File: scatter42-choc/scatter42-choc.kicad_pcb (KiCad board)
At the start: 2 copper layers, 260.1 x 107.6 mm, 112 parts, among them J0 MJ-4PP-9, J1 MJ-4PP-9, SW0 SW_PUSH, SW1 SW_PUSH, SW10 SW_PUSH, SW11 SW_PUSH, SW12 SW_PUSH, SW13 SW_PUSH, SW14 SW_PUSH, SW15 SW_PUSH, SW16 SW_PUSH, SW17 SW_PUSH, SW18 SW_PUSH, SW19 SW_PUSH, SW2 SW_PUSH, SW20 SW_PUSH, SW21 SW_PUSH, SW22 SW_PUSH, SW23 SW_PUSH, SW24 SW_PUSH, SW25 SW_PUSH, SW26 SW_PUSH, SW27 SW_PUSH, SW28 SW_PUSH, SW29 SW_PUSH, SW3 SW_PUSH, SW30 SW_PUSH, SW31 SW_PUSH, SW32 SW_PUSH, SW33 SW_PUSH, SW34 SW_PUSH, SW35 SW_PUSH, SW36 SW_PUSH, SW37 SW_PUSH, SW38 SW_PUSH, SW39 SW_PUSH, SW4 SW_PUSH, SW40 SW_PUSH, SW41 SW_PUSH, SW5 SW_PUSH, SW6 SW_PUSH, SW7 SW_PUSH, SW8 SW_PUSH, SW9 SW_PUSH, U0 ProMicro, U1 ProMicro

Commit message: mod cutline and silk
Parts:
- moved J1 0.71 mm to (160.5, 64.4)
- moved RSW1 0.68 mm to (165.1, 70.7)
- moved U1 0.52 mm to (169.5, 90.3)
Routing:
- net row0: track 215.4 -> 127.5 mm, vias 1 -> 0
- net row0_r: track 160.1 -> 112.4 mm
- net row1_r: track 147.3 -> 101.9 mm, vias 3 -> 0
- net row2_r: track 151.3 -> 108.6 mm, vias 3 -> 0
- net row3_r: track 202.5 -> 163.6 mm, vias 5 -> 1
- net col1: track 144.1 -> 164.0 mm, vias 1 -> 2
- net col4_r: track 108.9 -> 125.2 mm, vias 0 -> 2
- net row3: track 261.8 -> 248.4 mm, vias 5 -> 0
- net row2: track 140.2 -> 128.3 mm, vias 5 -> 3
- net col3: track 117.5 -> 128.3 mm, vias 0 -> 2
- net reset: track 35.6 -> 45.5 mm, vias 0 -> 1
- net Net-(D33-Pad2): track 21.7 -> 12.8 mm, vias 1 -> 0
- net col2: track 130.7 -> 122.0 mm, vias 0 -> 1
- net Net-(D29-Pad2): track 16.4 -> 24.6 mm, vias 1 -> 0
- net col5: track 55.6 -> 62.9 mm
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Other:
- outline, holes or cut-outs redrawn
- board text added: "Scatter42-Choc v1.0.1: PCB designed by @bbrfkr"
- board text removed: "Scatter42-Choc v1.0.0: PCB designed by @bbrfkr"

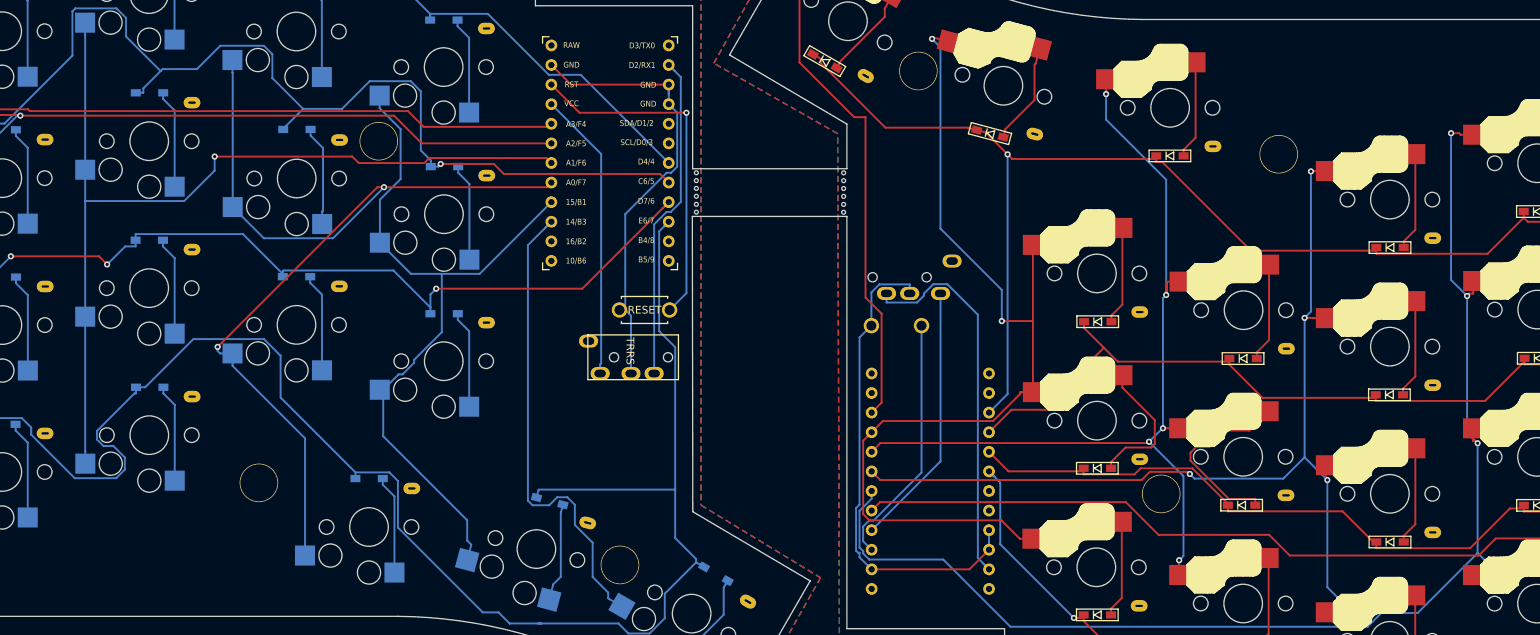
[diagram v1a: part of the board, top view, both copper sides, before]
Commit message: paste logo to pcb
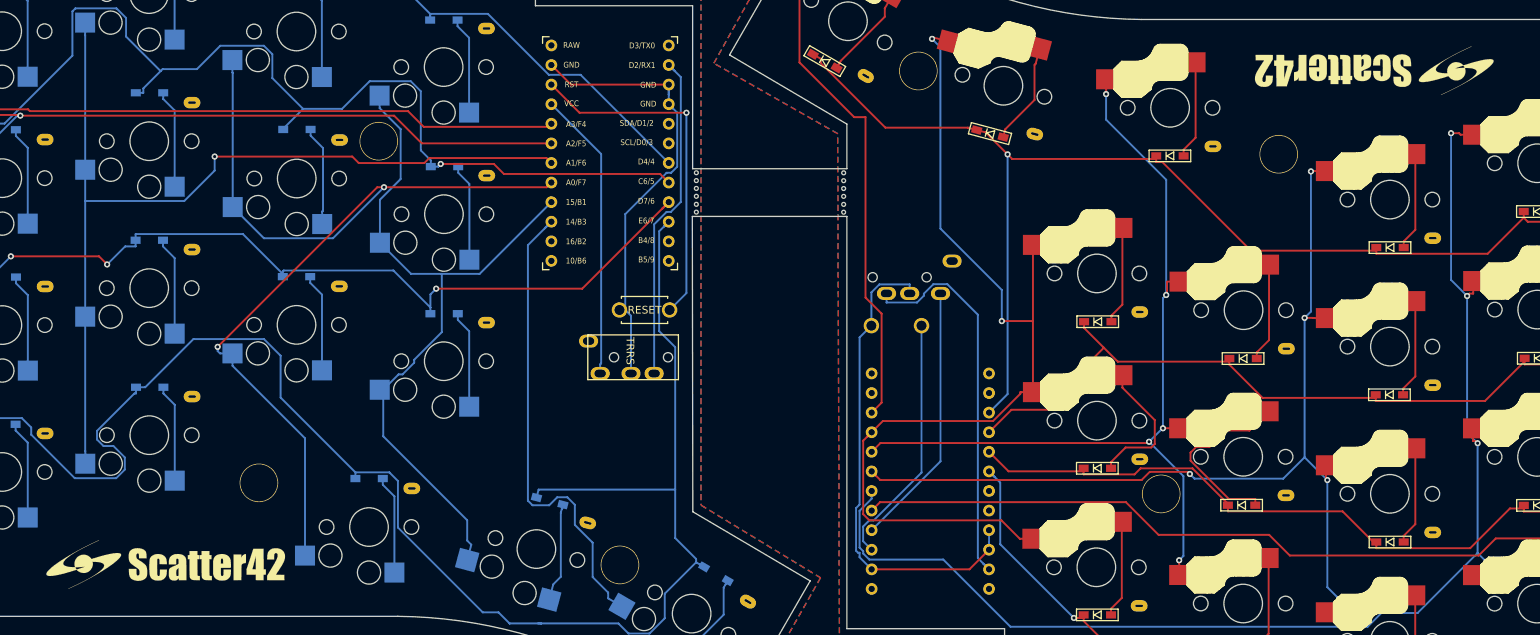
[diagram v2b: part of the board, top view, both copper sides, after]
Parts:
- added G***: LOGO, bbrfkr_logos:logo, B.Cu at (227.0, 37.6)
- added G***: LOGO, bbrfkr_logos:logo, F.Cu at (227.0, 37.6)
- added G***: LOGO, bbrfkr_logos:logo, B.Cu at (70.3, 101.6)
- added G***: LOGO, bbrfkr_logos:logo, F.Cu at (70.3, 101.6)
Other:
- board text added: "Scatter42-Choc v1.0.2: PCB designed by @bbrfkr"
- board text removed: "Scatter42-Choc v1.0.1: PCB designed by @bbrfkr"
